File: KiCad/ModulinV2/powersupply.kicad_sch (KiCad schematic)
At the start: 47 parts, among them IC40 REF196GSZ-REEL, IC41 NCP5500DADJR2G, IC42 LM2576S-12_NOPB, IC43 LM2576S-12_NOPB, IC44 REF195ESZ-REEL, IC45 NCP5500DADJR2G, IC46 L7812CD2T-TR, IC47 L7812CD2T-TR, J9 PJ-002B, Q3 DMP610DL-7

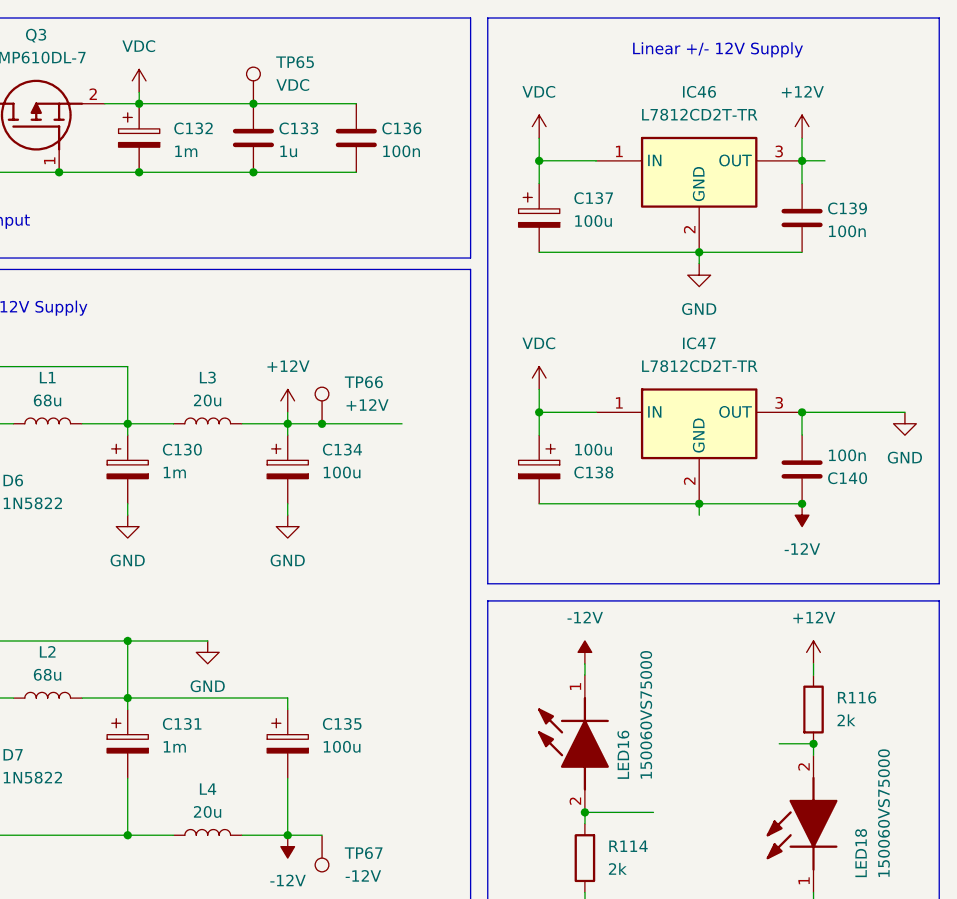
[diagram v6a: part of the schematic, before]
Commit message: Completed tuning & mod wheel layouts
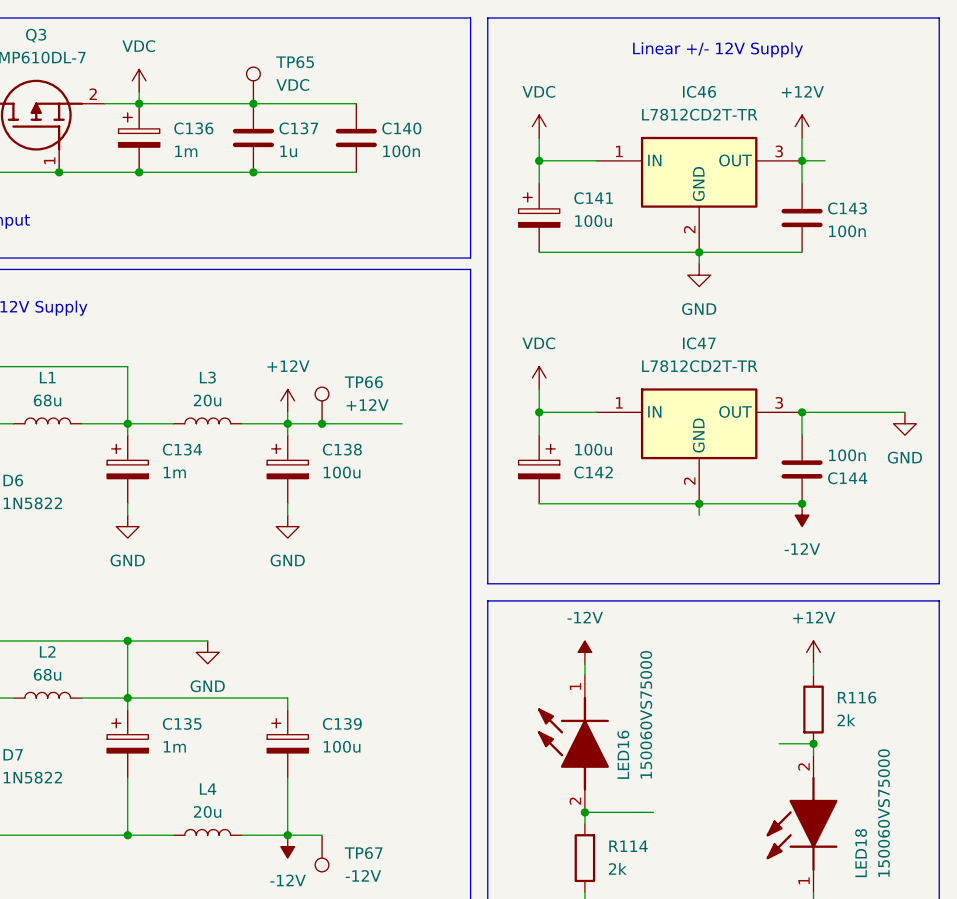
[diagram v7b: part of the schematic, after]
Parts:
- renumbered C130 to C134, C131 to C135, C132 to C136, C133 to C137, C134 to C138, C135 to C139, C136 to C140, C137 to C141, C138 to C142, C139 to C143, C140 to C144

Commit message: Fixed schematic connections
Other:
- company: (none) -> TalTech
- title: (none) -> Power supply
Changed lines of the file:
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@@
 	(paper "A4")
 	(title_block
+		(title "Power supply")
+		(date "2026-04-29")
+		(rev "1.4")
+		(company "TalTech")
 		(comment 1 "Instructor: Kaiser Pärnamets")
-		(comment 2 "By: Rasmus Palk")
+		(comment 2 "Author: Rasmus Palk")
 	)
 	(rectangle
